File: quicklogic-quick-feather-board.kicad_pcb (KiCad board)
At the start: 6 copper layers, 50.8 x 22.9 mm, 36 parts, among them IC1 EOS-S3, J5 0473460001, U1 TPS62821DLCR, U2 MCP73831T-2ACI_OT, U3 GD25Q16CWIGR, X1 ECS-_327-12_5-34B-TR

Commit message: Updated internal library
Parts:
- C1, C2, C4, C5: footprint antmicro-footprints:0603-cap -> quicklogic-quick-feather-board-footprints:0603-cap
- C3, C6, C7, C8, C9: footprint antmicro-footprints:0402-cap -> quicklogic-quick-feather-board-footprints:0402-cap
- D1: footprint antmicro-footprints:SOD-123 -> quicklogic-quick-feather-board-footprints:SOD-123
- D2: footprint antmicro-footprints:LED_0603 -> quicklogic-quick-feather-board-footprints:LED_0603
- IC1: footprint antmicro-footprints:42-WLCSP -> quicklogic-quick-feather-board-footprints:42-WLCSP
- J5: footprint antmicro-footprints:USB_Micro_B_Female_0473460001 -> quicklogic-quick-feather-board-footprints:USB_Micro_B_Female_0473460001
- L1: footprint antmicro-footprints:0805-res -> quicklogic-quick-feather-board-footprints:0805-res
- MIC1: footprint antmicro-footprints:IM69D130 -> quicklogic-quick-feather-board-footprints:IM69D130
- R1, R10, R11, R12, R13, R2, R3, R4, R5, R6, R7, R8, R9: footprint antmicro-footprints:0402-res -> quicklogic-quick-feather-board-footprints:0402-res
- TP1, TP2: footprint antmicro-footprints:Testpoint_smd_1mm -> quicklogic-quick-feather-board-footprints:Testpoint_smd_1mm
- U1: footprint antmicro-footprints:QFN-8_2x1mm -> quicklogic-quick-feather-board-footprints:QFN-8_2x1mm
- U2: footprint antmicro-footprints:SOT-753 -> quicklogic-quick-feather-board-footprints:SOT-753
- U3: footprint antmicro-footprints:GD25Q16CWIG -> quicklogic-quick-feather-board-footprints:GD25Q16CWIG
- X1: footprint antmicro-footprints:SMD-2_3.2x1.5mm -> quicklogic-quick-feather-board-footprints:SMD-2_3.2x1.5mm

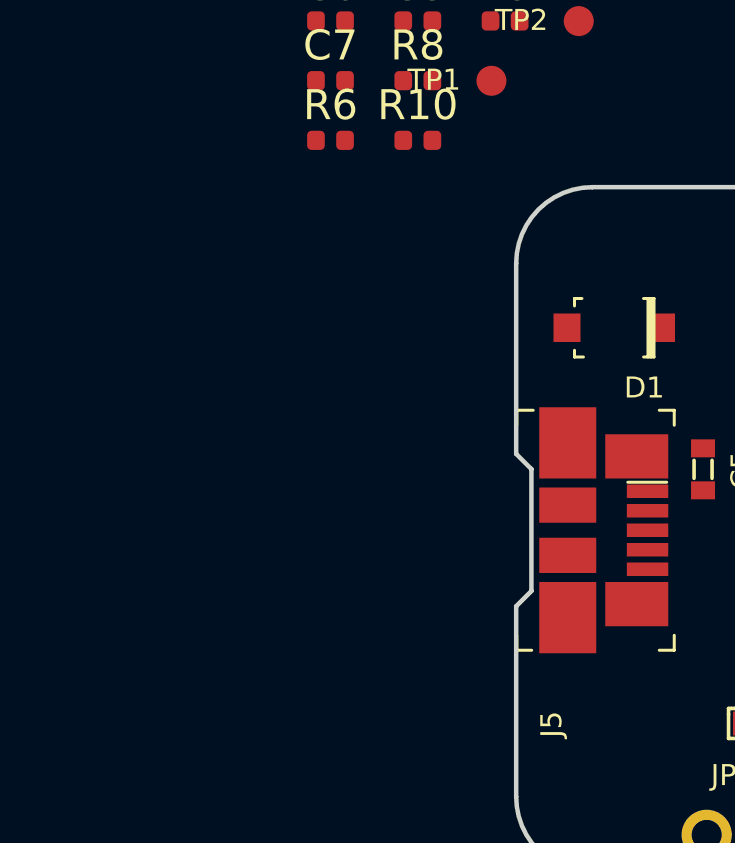
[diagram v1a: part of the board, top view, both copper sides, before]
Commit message: Added accelerometer and circuit for measuring battery voltage
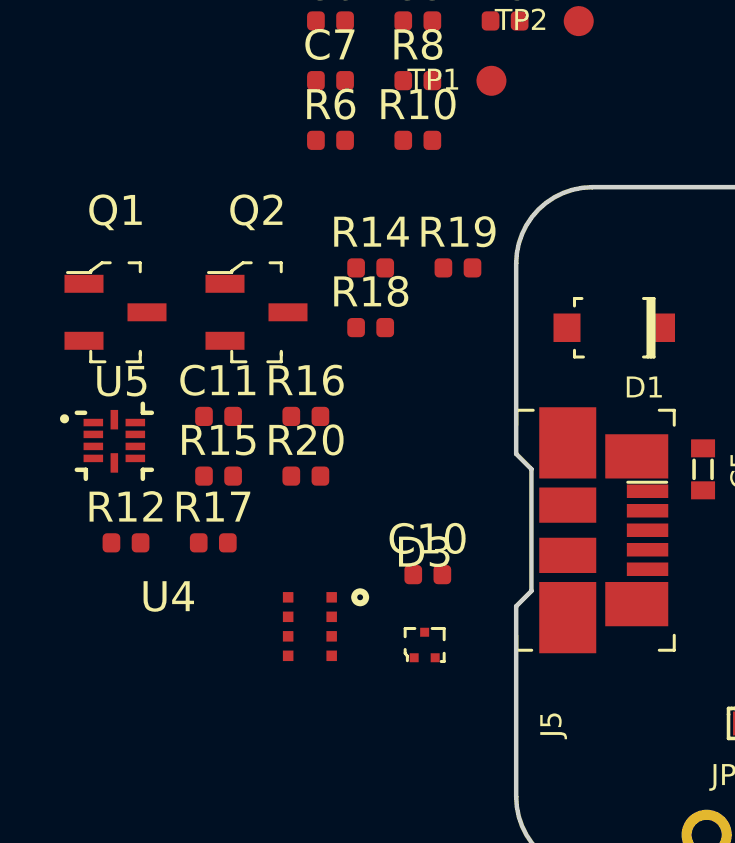
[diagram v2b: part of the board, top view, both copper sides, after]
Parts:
- added C10: C_100n_0402_6V3, quicklogic-quick-feather-board-footprints:0402-cap, F.Cu at (120.2, 106.5)
- added C11: C_100n_0402_6V3, quicklogic-quick-feather-board-footprints:0402-cap, F.Cu at (113.2, 101.2)
- added D3: TPD2EUSB30DRTR, quicklogic-quick-feather-board-footprints:SOT-3, F.Cu at (120.0, 108.8)
- added Q1: BSS138AKA, quicklogic-quick-feather-board-footprints:SOT-23-3, F.Cu at (109.7, 97.7)
- added Q2: BSS84, quicklogic-quick-feather-board-footprints:SOT-23-3, F.Cu at (114.4, 97.7)
- added R12: R_100k_1%_0402, quicklogic-quick-feather-board-footprints:0402-res, F.Cu at (110.1, 105.4)
- added R14: R_10k_0402, quicklogic-quick-feather-board-footprints:0402-res, F.Cu at (118.2, 96.3)
- added R15: R_10k_0402, quicklogic-quick-feather-board-footprints:0402-res, F.Cu at (113.2, 103.2)
- added R16: R_200k_0402, quicklogic-quick-feather-board-footprints:0402-res, F.Cu at (116.1, 101.2)
- added R17: R_100k_1%_0402, quicklogic-quick-feather-board-footprints:0402-res, F.Cu at (113.0, 105.4)
- added R18: R_10k_0402, quicklogic-quick-feather-board-footprints:0402-res, F.Cu at (118.2, 98.3)
- added R19: R_10k_0402, quicklogic-quick-feather-board-footprints:0402-res, F.Cu at (121.2, 96.3)
- added R20: R_10k_0402, quicklogic-quick-feather-board-footprints:0402-res, F.Cu at (116.1, 103.2)
- added U4: DPS310, quicklogic-quick-feather-board-footprints:PG-VLGA-8-2, F.Cu at (115.0, 106.2)
- added U5: MC3635, quicklogic-quick-feather-board-footprints:MC3635, F.Cu at (110.0, 102.0)
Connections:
- C1 pad 1: /VBUS -> +3V3
- C2 pad 1: /VBAT -> +3V3
- C3 pad 1: /3V3_SYS -> +3V3
- C4 pad 1: /3V3_SYS -> +3V3
- C5 pad 1: /VBUS -> +3V3
- C8 pad 1: /3V3_SYS -> +3V3
- C9 pad 2: Net-(C9-Pad2) -> +3V3
- D1 pad A: /VBAT -> +3V3
- D1 pad K: /VBUS -> +3V3
- D2 pad 1: /VBUS -> +3V3
- IC1 pad A7: Net-(IC1-PadA7) -> /I2C_SCL
- IC1 pad B2: Net-(IC1-PadB2) -> /ADC0
- IC1 pad B3: /3V3_SYS -> +3V3
- IC1 pad B7: Net-(IC1-PadB7) -> /I2C_SDA
- IC1 pad C2: /3V3_SYS -> +3V3
- IC1 pad C6: /3V3_SYS -> +3V3
- IC1 pad D6: /3V3_SYS -> +3V3
- IC1 pad D7: /INT -> /IMU_INT
- IC1 pad E4: /IO31 -> /ADC0_EN
- J5 pad 1: /VBUS -> +3V3
- L1 pad 2: /3V3_SYS -> +3V3
- MIC1 pad 2: /3V3_SYS -> +3V3
- R1 pad 1: /VBUS -> +3V3
- R10 pad 1: /3V3_SYS -> +3V3
- R10 pad 2: /SPI_WP -> /SPI_HOLD
- R4 pad 1: /3V3_SYS -> +3V3
- R6 pad 1: /3V3_SYS -> +3V3
- R8 pad 1: /SPI_HOLD -> +3V3
- R8 pad 2: /3V3_SYS -> /SPI_WP
- U1 pad 1: /VBUS -> +3V3
- U1 pad 7: /VBUS -> +3V3
- U2 pad 3: /VBAT -> +3V3
- U2 pad 4: /VBUS -> +3V3
- U3 pad 8: /3V3_SYS -> +3V3
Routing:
- net /3V3_SYS: track 6.55 -> 0.00 mm, vias 4 -> 0
- net +3V3: track 0.00 -> 6.55 mm, vias 4 -> 8
- net /INT: track 2.57 -> 0.00 mm
- net /IMU_INT: track 0.00 -> 2.57 mm
- net Net-(IC1-PadB7): track 2.28 -> 0.00 mm
- net /I2C_SDA: track 0.00 -> 2.28 mm
- net Net-(IC1-PadB2): track 2.24 -> 0.00 mm, vias 1 -> 0
- net /ADC0: track 0.00 -> 2.24 mm, vias 0 -> 1
- net /IO31: track 2.16 -> 0.00 mm, vias 1 -> 0
- net /ADC0_EN: track 0.00 -> 2.16 mm, vias 0 -> 1
- net Net-(IC1-PadA7): track 1.81 -> 0.00 mm
- net /I2C_SCL: track 0.00 -> 1.81 mm

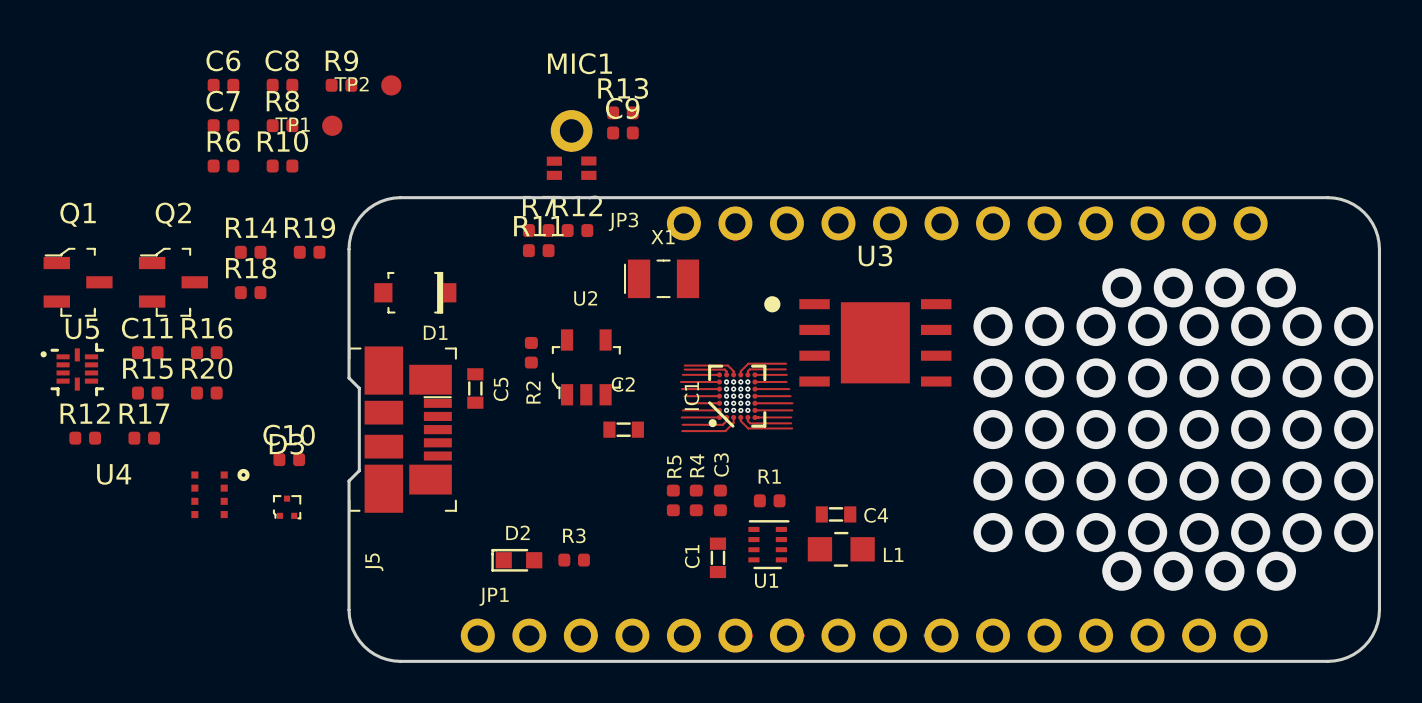
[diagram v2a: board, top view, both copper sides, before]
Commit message: Added bootstrap resistors, connected pressure sensor to I2C bus, placed components on PCB
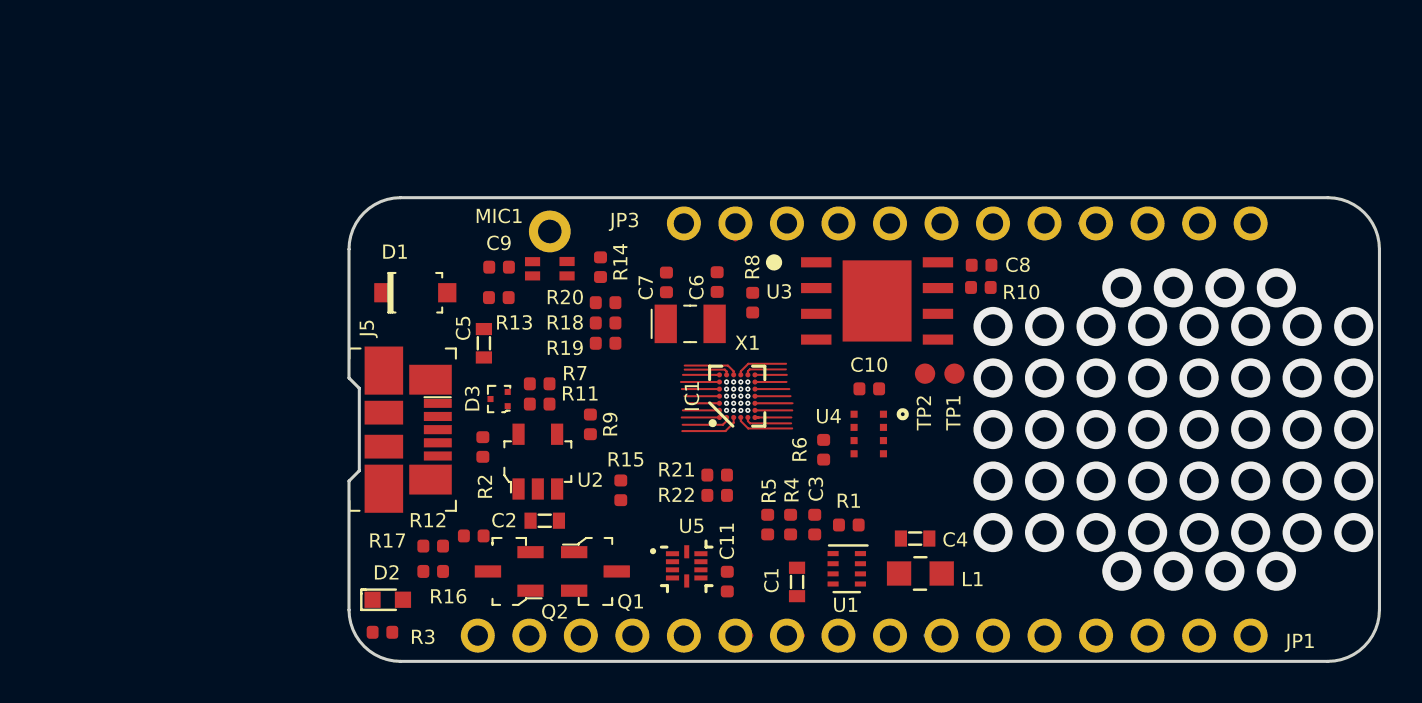
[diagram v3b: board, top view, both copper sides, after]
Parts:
- removed the R12 at (110.1, 105.4)
- removed the R12 at (134.4, 95.2)
- added R12: R_100k_1%_0402, quicklogic-quick-feather-board-footprints:0402-res, F.Cu at (129.2, 110.2)
- added R21: R_10k_0402, quicklogic-quick-feather-board-footprints:0402-res, F.Cu at (141.2, 107.2)
- added R22: R_10k_0402, quicklogic-quick-feather-board-footprints:0402-res, F.Cu at (141.2, 108.2)
- moved C8 35.6 mm to (154.3, 96.9)
- moved R10 34.9 mm to (154.2, 98.0), turned to 180 degrees
- moved TP1 33.0 mm to (153.0, 102.2), turned to 90 degrees
- moved R6 32.7 mm to (146.5, 106.0), turned to 90 degrees
- moved U4 32.6 mm to (147.5, 103.2)
- moved U5 31.6 mm to (140.0, 111.8)
- moved C11 30.7 mm to (141.8, 112.5), turned to 270 degrees
- moved TP2 29.9 mm to (151.6, 102.2), turned to 90 degrees
- moved Q1 29.2 mm to (135.2, 112.0)
- moved C10 28.8 mm to (148.8, 103.0)
- moved C6 26.2 mm to (141.2, 97.7), turned to 90 degrees
- moved R8 24.8 mm to (143.0, 98.8), turned to 270 degrees
- moved R15 23.8 mm to (136.5, 108.0), turned to 270 degrees
- moved C7 23.2 mm to (138.8, 97.8), turned to 90 degrees
- moved Q2 21.8 mm to (131.0, 112.0), turned to 180 degrees
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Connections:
- C1 pad 1: +3V3 -> +VBUS
- C2 pad 1: +3V3 -> +VBAT
- C5 pad 1: +3V3 -> +VBUS
- D1 pad A: +3V3 -> +VBAT
- D1 pad K: +3V3 -> +VBUS
- D2 pad 1: +3V3 -> +VBUS
- J5 pad 1: +3V3 -> +VBUS
- JP1 pad 1: GND -> (no net)
- JP1 pad 10: A2 -> (no net)
- JP1 pad 11: A1 -> (no net)
- JP1 pad 12: A0 -> (no net)
- JP1 pad 13: GND -> (no net)
- JP1 pad 14: AREF -> (no net)
- JP1 pad 15: +3V3 -> (no net)
- JP1 pad 16: ~RESET -> (no net)
- JP1 pad 2: D1 -> (no net)
- JP1 pad 3: D0 -> (no net)
- JP1 pad 4: MISO -> (no net)
- JP1 pad 5: MOSI -> (no net)
- JP1 pad 6: SCK -> (no net)
- JP1 pad 7: A5 -> (no net)
- JP1 pad 8: A4 -> (no net)
- JP1 pad 9: A3 -> (no net)
- JP3 pad 1: VBAT -> (no net)
- JP3 pad 10: D5 -> (no net)
- JP3 pad 11: SCL -> (no net)
- JP3 pad 12: SDA -> (no net)
- JP3 pad 2: EN -> (no net)
- JP3 pad 3: VBUS -> (no net)
- JP3 pad 4: D13 -> (no net)
- JP3 pad 5: D12 -> (no net)
- JP3 pad 6: D11 -> (no net)
- JP3 pad 7: D10 -> (no net)
- JP3 pad 8: D9 -> (no net)
- JP3 pad 9: D6 -> (no net)
- Q2 pad 2: +3V3 -> +VBAT
- R1 pad 1: +3V3 -> +VBUS
- U1 pad 1: +3V3 -> +VBUS
- U1 pad 7: +3V3 -> +VBUS
- U2 pad 3: +3V3 -> +VBAT
- U2 pad 4: +3V3 -> +VBUS
- U4 pad 2: /SPI_MST_SS -> Net-(U4-Pad2)
- U4 pad 3: /SPI_MST_MOSI -> /I2C_SDA
- U4 pad 4: /SPI_MST_CLK -> /I2C_SCL
- U4 pad 5: /SPI_MST_MISO -> Net-(U4-Pad5)
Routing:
- net (no net): track 0.00 -> 7.93 mm, vias 0 -> 48
- net A2: track 1.02 -> 0.00 mm
- net AREF: track 0.89 -> 0.00 mm
- net EN: track 0.76 -> 0.00 mm
- net D6: track 0.76 -> 0.00 mm
- net A5: track 0.76 -> 0.00 mm
- net A1: track 0.76 -> 0.00 mm
- net D11: track 0.64 -> 0.00 mm
- net SCL: track 0.63 -> 0.00 mm
- net D5: track 0.51 -> 0.00 mm
- net D13: track 0.51 -> 0.00 mm
- net D12: track 0.51 -> 0.00 mm
- net N$9: vias 1 -> 0
- net N$8: vias 1 -> 0
- net N$6: vias 1 -> 0
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- removed copper zone on In3.Cu, net /3V3_SYS

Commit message: Design updated after internal review
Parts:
- removed JP1: , 1X16_ROUND
- removed JP3: , 1X12_ROUND
- added C12: C_100n_0402_6V3, antmicro-footprints:0402-cap, F.Cu at (154.6, 84.7)
- added C13: C_100n_0402_6V3, antmicro-footprints:0402-cap, F.Cu at (154.6, 82.7)
- added C14: C_4u7_0603, quicklogic-quick-feather-board-footprints:0603-cap, F.Cu at (175.3, 67.0)
- added C15: C_100n_0402_6V3, antmicro-footprints:0402-cap, F.Cu at (178.5, 66.8)
- added C16: C_4u7_0603, quicklogic-quick-feather-board-footprints:0603-cap, F.Cu at (154.9, 80.5)
- added C17: C_100n_0402_6V3, antmicro-footprints:0402-cap, F.Cu at (157.5, 82.7)
- added D10: TPD2EUSB30DRTR, quicklogic-quick-feather-board-footprints:SOT-3, F.Cu at (125.4, 79.2)
- added D11: TPD2EUSB30DRTR, quicklogic-quick-feather-board-footprints:SOT-3, F.Cu at (122.7, 84.6)
- added D4: UHD1110-FKA, quicklogic-quick-feather-board-footprints:LED-RGB-5DS-UHD1110-FKA, F.Cu at (174.6, 69.4)
- added D5: TPD2EUSB30DRTR, quicklogic-quick-feather-board-footprints:SOT-3, F.Cu at (120.0, 79.2)
- added D6: TPD2EUSB30DRTR, quicklogic-quick-feather-board-footprints:SOT-3, F.Cu at (120.0, 81.9)
- added D7: TPD2EUSB30DRTR, quicklogic-quick-feather-board-footprints:SOT-3, F.Cu at (122.7, 79.2)
- added D8: TPD2EUSB30DRTR, quicklogic-quick-feather-board-footprints:SOT-3, F.Cu at (120.0, 84.6)
- added D9: TPD2EUSB30DRTR, quicklogic-quick-feather-board-footprints:SOT-3, F.Cu at (122.7, 81.9)
- added J1: SHF-105-01-L-D-SM, quicklogic-quick-feather-board-footprints:SHF-105-01-L-D-SM, F.Cu at (147.3, 79.2)
- added J2: 1x12_pinhead, quicklogic-quick-feather-board-footprints:1x12_pinhead, F.Cu at (139.5, 92.2)
- added J3: 1x16_pinhead, quicklogic-quick-feather-board-footprints:1x16_pinhead, F.Cu at (167.6, 115.1)
- added R18: R_4k7_0402, quicklogic-quick-feather-board-footprints:0402-res, F.Cu at (161.1, 80.2)
- added R20: R_4k7_0402, quicklogic-quick-feather-board-footprints:0402-res, F.Cu at (158.2, 80.2)
- added R23: R_10k_0402, quicklogic-quick-feather-board-footprints:0402-res, F.Cu at (154.6, 86.7)
- added S1: TL3365AF180QG, quicklogic-quick-feather-board-footprints:SW_SPST_4.2x3.2, F.Cu at (117.8, 89.1)
- added S1: PTS645SM43SMTR92_LFS, quicklogic-quick-feather-board-footprints:Switch_Tactile_SMD_6x6mm_PTS645, F.Cu at (169.7, 75.5)
- added S2: TL3365AF180QG, quicklogic-quick-feather-board-footprints:SW_SPST_4.2x3.2, F.Cu at (125.0, 89.1)
- added S2: PTS645SM43SMTR92_LFS, quicklogic-quick-feather-board-footprints:Switch_Tactile_SMD_6x6mm_PTS645, F.Cu at (158.7, 75.5)
- added TP3: TP_SMD1MM, quicklogic-quick-feather-board-footprints:Testpoint_smd_1mm, F.Cu at (157.1, 84.8)
- added TP4: TP_SMD1MM, quicklogic-quick-feather-board-footprints:Testpoint_smd_1mm, F.Cu at (163.5, 80.3)
- added TP5: TP_SMD1MM, quicklogic-quick-feather-board-footprints:Testpoint_smd_1mm, F.Cu at (160.0, 82.3)
- added TP6: TP_SMD1MM, quicklogic-quick-feather-board-footprints:Testpoint_smd_1mm, F.Cu at (176.2, 71.5)
- added TP7: TP_SMD1MM, quicklogic-quick-feather-board-footprints:Testpoint_smd_1mm, F.Cu at (160.0, 84.3)
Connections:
- net /RST_N renamed /SYS_RST
- net /SPI_SLV_MOSI renamed /HEADER_MOSI
- net Net-(IC1-PadA2) renamed /VDD1
- net Net-(IC1-PadA3) renamed /VDD2
- IC1 pad A4: Net-(IC1-PadA4) -> /SWD_CLK
- IC1 pad A6: Net-(IC1-PadA6) -> /HEADER_P5
- IC1 pad B4: Net-(IC1-PadB4) -> /SDW_IO
- IC1 pad C7: Net-(IC1-PadC7) -> /HEADER_P6
- IC1 pad D1: /SPI_SLV_MISO -> /HEADER_MISO
- IC1 pad D2: /IO24 -> /LED_R
- IC1 pad D3: /IO25 -> /LED_G
- IC1 pad E1: /SPI_SLV_CLK -> /HEADER_SCK
- IC1 pad E7: /SDW_IO -> /USR_BUTTON
- IC1 pad F2: /SPI_SLV_SS -> /HEADER_A5
- IC1 pad F4: /IO30 -> /LED_B
- IC1 pad F7: /SWD_CLK -> /HEADER_P7
- R21 pad 1: GND -> /HEADER_A5
- R21 pad 2: /SPI_SLV_SS -> GND
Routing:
- net (no net): track 7.93 -> 0.00 mm
- net /HEADER_P6: track 0.00 -> 3.22 mm
- net /HEADER_SCK: track 0.00 -> 3.12 mm
- net /LED_R: track 0.00 -> 2.92 mm, vias 0 -> 1
- net /IO24: track 2.92 -> 0.00 mm, vias 1 -> 0
- net /SPI_SLV_MISO: track 2.86 -> 0.00 mm
- net /HEADER_MISO: track 0.00 -> 2.86 mm
- net /HEADER_A5: track 0.00 -> 2.86 mm
- net Net-(IC1-PadC7): track 2.71 -> 0.00 mm
- net Net-(IC1-PadB4): track 2.37 -> 0.00 mm, vias 1 -> 0
- net /SPI_SLV_CLK: track 2.36 -> 0.00 mm
- net /USR_BUTTON: track 0.00 -> 2.09 mm
- net /HEADER_P7: track 0.00 -> 2.08 mm
- net Net-(IC1-PadA6): track 1.90 -> 0.00 mm
- net /HEADER_P5: track 0.00 -> 1.90 mm
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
